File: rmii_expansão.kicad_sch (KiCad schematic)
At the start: 6 parts, among them CN3 100nf, J19 Bus_PCI_Express_Mini

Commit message: 21082026/G
falta muita coisa
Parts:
- removed J19: Bus_PCI_Express_Mini, Connector_PCBEdge:BUS_PCI_Express_Mini_Full, symbol Connector:Bus_PCI_Express_Mini
- added J19: ETH, symbol Connector_Generic:Conn_02x10_Row_Letter_First
- renumbered C102 to C100, D8 to D7
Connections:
- net GND: now also J19.a10 (Pin_a10), J19.a2 (Pin_a2), J19.a4 (Pin_a4), J19.a6 (Pin_a6), J19.a8 (Pin_a8), J19.b10 (Pin_b10), J19.b2 (Pin_b2), J19.b4 (Pin_b4), J19.b6 (Pin_b6), J19.b8 (Pin_b8)
- net SUB_RMII_CRS_DV: now also J19.a5 (Pin_a5)
- net SUB_RMII_RXD0: now also J19.b5 (Pin_b5)
- net SUB_RMII_RXD1: now also J19.a7 (Pin_a7)
- net SUB_RMII_TXD0: now also J19.a9 (Pin_a9)
- net SUB_RMII_TXD1: now also J19.b3 (Pin_b3)
- net SUB_RMII_TXEN: now also J19.a3 (Pin_a3)
- net vcc_RMII: now also J19.a1 (Pin_a1), J19.b1 (Pin_b1)
- new net SUB_GPIO_1: J19.b7 (Pin_b7)
- new net SUB_GPIO_2: J19.b9 (Pin_b9)
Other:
- moved on the sheet: D7, F11

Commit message: 29082026/I
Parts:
- CN3: jlc_pcb: C346191 -> C307348; mouser: (none) -> 187-CL10B104KB8WPNC; mpn CA0612MRX7R7BB104 -> CL10B104KB8WPNC
- J19: footprint (none) -> Connector_PinHeader_2.54mm:PinHeader_2x10_P2.54mm_Horizontal; Descrição (none) -> o da lcsc e da mouser sâo diferente; jlc_pcb: (none) -> C53207373; mouser: (none) -> 649-68021-120HLF; mpn (none) -> PZ-2.54-2*10-8.5-WZ
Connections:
- net GND: now also J19.a9 (Pin_a9), J19.b1 (Pin_b1), J19.b3 (Pin_b3), J19.b5 (Pin_b5), J19.b7 (Pin_b7), J19.b9 (Pin_b9); no longer J19.a10 (Pin_a10), J19.b10 (Pin_b10), J19.b2 (Pin_b2), J19.b4 (Pin_b4), J19.b6 (Pin_b6), J19.b8 (Pin_b8)
- net SUB_GPIO_1: now also J19.b6 (Pin_b6); no longer J19.b7 (Pin_b7)
- net SUB_GPIO_2: now also J19.b8 (Pin_b8); no longer J19.b9 (Pin_b9)
- net SUB_RMII_CRS_DV: now also J19.a3 (Pin_a3); no longer J19.a5 (Pin_a5)
- net SUB_RMII_RXD0: now also J19.b4 (Pin_b4); no longer J19.b5 (Pin_b5)
- net SUB_RMII_RXD1: now also J19.a5 (Pin_a5); no longer J19.a7 (Pin_a7)
- net SUB_RMII_TXD0: now also J19.a7 (Pin_a7); no longer J19.a9 (Pin_a9)
- net SUB_RMII_TXD1: now also J19.b2 (Pin_b2); no longer J19.b3 (Pin_b3)
- net SUB_RMII_TXEN: now also J19.a1 (Pin_a1); no longer J19.a3 (Pin_a3)
- net vcc_RMII: now also J19.a10 (Pin_a10), J19.b10 (Pin_b10); no longer J19.a1 (Pin_a1), J19.b1 (Pin_b1)
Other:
- company: (none) -> ---
- title: (none) -> expansão com ethernet
- moved on the sheet: D7, F11, J19

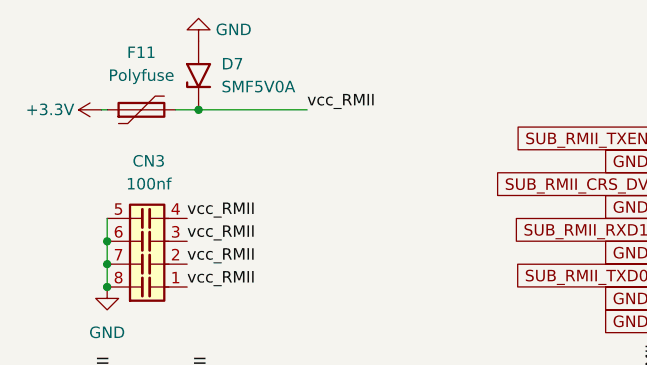
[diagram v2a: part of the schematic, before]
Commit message: o .bom não foi terminado
O desafio e todo custar menos de 150 dólares(eua) e menos de 1000r(reais)
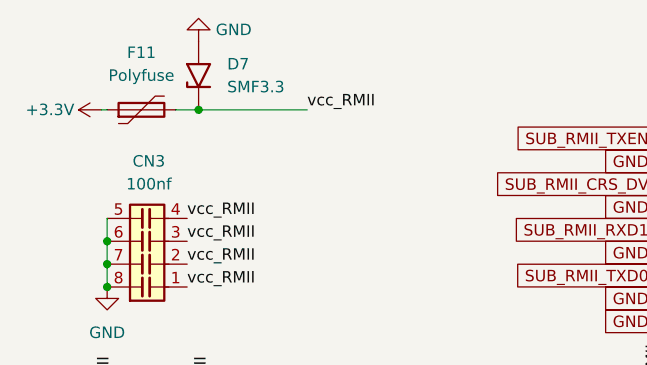
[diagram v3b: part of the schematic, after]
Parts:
- C100, C99: footprint (none) -> Capacitor_SMD:C_1206_3216Metric_Pad1.33x1.80mm_HandSolder; jlc_pcb: (none) -> C13585; mouser: (none) -> 187-CL31B106KLK6PNE; mpn (none) -> CL31A106KBHNNNE
- D7: value SMF5V0A -> SMF3.3
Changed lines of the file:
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@@
+	)
+	(junction
+		(at 33.02 33.02)
+		(diameter 0)
+		(color 0 0 0 0)
 	)
 	(junction
@@
 	)
 	(junction
-		(at 33.02 33.02)
-		(diameter 0)
-		(color 0 0 0 0)
-	)
-	(junction
 		(at 22.86 50.165)
 		(diameter 0)
@@
 	(wire
 		(pts
-			(xy 33.02 33.02) (xy 45.085 33.02)
+			(xy 30.48 33.02) (xy 33.02 33.02)
 		)
 		(stroke
@@
 	(wire
 		(pts
-			(xy 33.02 33.02) (xy 30.48 33.02)
+			(xy 22.86 50.165) (xy 22.86 52.705)
 		)
 		(stroke
@@
 	(wire
 		(pts
-			(xy 22.86 50.165) (xy 22.86 52.705)
+			(xy 33.02 33.02) (xy 45.085 33.02)
 		)
 		(stroke
@@
 	)
 	(symbol
+		(lib_id "Diode:SMF5V0A")
+		(at 33.02 29.21 90)
+		(unit 1)
+		(body_style 1)
+		(exclude_from_sim no)
+		(in_bom yes)
+		(on_board yes)
+		(in_pos_files yes)
+		(dnp no)
+		(fields_autoplaced yes)
+		(property "Reference" "D7"
+			(at 36.195 27.9399 90)
+			(show_name no)
+			(do_not_autoplace no)
+			(effects
+				(font
+					(size 1.27 1.27)
+				)
+				(justify right)
+			)
+		)
+		(property "Value" "SMF3.3"
+			(at 36.195 30.4799 90)
+			(show_name no)
+			(do_not_autoplace no)
+			(effects
+				(font
+					(size 1.27 1.27)
+				)
+				(justify right)
+			)
+		)
+		(property "Footprint" "Diode_SMD:D_SMF"
+			(at 38.1 29.21 0)
+			(hide yes)
+			(show_name no)
+			(do_not_autoplace no)
+			(effects
+				(font
+					(size 1.27 1.27)
+				)
+			)
+		)
+		(property "Datasheet" "https://www.vishay.com/doc?85881"
+			(at 33.02 30.48 0)
+			(hide yes)
+			(show_name no)
+			(do_not_autoplace no)
+			(effects
+				(font
+					(size 1.27 1.27)
+				)
+			)
+		)
+		(property "Description" "200W unidirectional Transil Transient Voltage Suppressor, 5Vrwm, SMF"
+			(at 33.02 29.21 0)
+			(hide yes)
+			(show_name no)
+			(do_not_autoplace no)
+			(effects
+				(font
+					(size 1.27 1.27)
+				)
+			)
+		)
+		(property "jlc_pcb:" ""
+			(at 33.02 29.21 0)
+			(hide yes)
+			(show_name no)
+			(do_not_autoplace no)
+			(effects
+				(font
+					(size 1.27 1.27)
+				)
+			)
+		)
+		(property "mpn" ""
+			(at 33.02 29.21 0)
+			(hide yes)
+			(show_name no)
+			(do_not_autoplace no)
+			(effects
+				(font
+					(size 1.27 1.27)
+				)
+			)
+		)
+		(property "mouser:" ""
+			(at 33.02 29.21 0)
+			(hide yes)
+			(show_name no)
+			(do_not_autoplace no)
+			(effects
+				(font
+					(size 1.27 1.27)
+				)
+			)
+		)
+		(property "Descrição" ""
+			(at 33.02 29.21 0)
+			(hide yes)
+			(show_name no)
+			(do_not_autoplace no)
+			(effects
+				(font
+					(size 1.27 1.27)
+				)
+			)
+		)
+		(pin "2"
+		)
+		(pin "1"
+		)
+		(instances
+			(project "hapia"
+				(path "/03882c7f-4c9a-440f-b893-3aa618650b49"
+					(reference "D7")
+					(unit 1)
+				)
+			)
+		)
+	)
+	(symbol
 		(lib_id "Device:C_Network04")
 		(at 27.94 47.625 90)
@@
 	)
 	(symbol
-		(lib_id "Diode:SMF5V0A")
-		(at 33.02 29.21 90)
-		(unit 1)
-		(body_style 1)
-		(exclude_from_sim no)
-		(in_bom yes)
-		(on_board yes)
-		(in_pos_files yes)
-		(dnp no)
-		(fields_autoplaced yes)
-		(property "Reference" "D7"
-			(at 35.56 27.9399 90)
-			(show_name no)
-			(do_not_autoplace no)
-			(effects
-				(font
-					(size 1.27 1.27)
-				)
-				(justify right)
-			)
-		)
-		(property "Value" "SMF5V0A"
-			(at 35.56 30.4799 90)
-			(show_name no)
-			(do_not_autoplace no)
-			(effects
-				(font
-					(size 1.27 1.27)
-				)
-				(justify right)
-			)
-		)
-		(property "Footprint" "Diode_SMD:D_SMF"
-			(at 38.1 29.21 0)
-			(hide yes)
-			(show_name no)
-			(do_not_autoplace no)
-			(effects
-				(font
-					(size 1.27 1.27)
-				)
-			)
-		)
-		(property "Datasheet" "https://www.vishay.com/doc?85881"
-			(at 33.02 30.48 0)
-			(hide yes)
-			(show_name no)
-			(do_not_autoplace no)
-			(effects
-				(font
-					(size 1.27 1.27)
-				)
-			)
-		)
-		(property "Description" "200W unidirectional Transil Transient Voltage Suppressor, 5Vrwm, SMF"
-			(at 33.02 29.21 0)
-			(hide yes)
-			(show_name no)
-			(do_not_autoplace no)
-			(effects
-				(font
-					(size 1.27 1.27)
-				)
-			)
-		)
-		(pin "2"
-		)
-		(pin "1"
-		)
-		(instances
-			(project "hapia"
-				(path "/03882c7f-4c9a-440f-b893-3aa618650b49"
-					(reference "D7")
-					(unit 1)
-				)
-			)
-		)
-	)
-	(symbol
 		(lib_id "Device:C")
 		(at 34.29 71.755 0)
@@
 			)
 		)
-		(property "Footprint" ""
+		(property "Footprint" "Capacitor_SMD:C_1206_3216Metric_Pad1.33x1.80mm_HandSolder"
 			(at 35.2552 75.565 0)
 			(hide yes)
@@
 			)
 		)
-		(property "Datasheet" ""
+		(property "Datasheet" "https://www.lcsc.com/datasheet/C13585.pdf?spm=wm.sxq.inf.ggs___wm.fly.bg.1.xh&lcsc_vid=RFYLUFJeFgBYVgUARVEKU1ZUEwNcUQJQEVkIVlNSQgIxVlNeQFhbU1VUQFRWUTsOAxUeFF5JWBYZEEoKFBINSQcJGk4NBhADEA4cHktRR1NADxALGw%3D%3D"
 			(at 34.29 71.755 0)
 			(hide yes)
@@
 		)
 		(property "Description" "Unpolarized capacitor"
+			(at 34.29 71.755 0)
+			(hide yes)
+			(show_name no)
+			(do_not_autoplace no)
+			(effects
+				(font
+					(size 1.27 1.27)
+				)
+			)
+		)
+		(property "jlc_pcb:" "C13585"
+			(at 34.29 71.755 0)
+			(hide yes)
+			(show_name no)
+			(do_not_autoplace no)
+			(effects
+				(font
+					(size 1.27 1.27)
+				)
+			)
+		)
+		(property "mouser:" "187-CL31B106KLK6PNE"
+			(at 34.29 71.755 0)
+			(hide yes)
+			(show_name no)
+			(do_not_autoplace no)
+			(effects
+				(font
+					(size 1.27 1.27)
+				)
+			)
+		)
+		(property "mpn" "CL31A106KBHNNNE"
 			(at 34.29 71.755 0)
 			(hide yes)
@@
 			)
 		)
-		(property "Footprint" ""
+		(property "Footprint" "Capacitor_SMD:C_1206_3216Metric_Pad1.33x1.80mm_HandSolder"
 			(at 24.4602 75.565 0)
 			(hide yes)
@@
 			)
 		)
-		(property "Datasheet" ""
+		(property "Datasheet" "https://www.lcsc.com/datasheet/C13585.pdf?spm=wm.sxq.inf.ggs___wm.fly.bg.1.xh&lcsc_vid=RFYLUFJeFgBYVgUARVEKU1ZUEwNcUQJQEVkIVlNSQgIxVlNeQFhbU1VUQFRWUTsOAxUeFF5JWBYZEEoKFBINSQcJGk4NBhADEA4cHktRR1NADxALGw%3D%3D"
 			(at 23.495 71.755 0)
 			(hide yes)
@@
 			(at 23.495 71.755 0)
 			(hide yes)
+			(show_name no)
+			(do_not_autoplace no)
+			(effects
+				(font
+					(size 1.27 1.27)
+				)
+			)
+		)
+		(property "jlc_pcb:" "C13585"
+			(at 23.495 71.755 0)
+			(hide yes)
+			(show_name no)
+			(do_not_autoplace no)
+			(effects
+				(font
+					(size 1.27 1.27)
+				)
+			)
+		)
+		(property "mouser:" "187-CL31B106KLK6PNE"
+			(at 23.495 71.755 0)
+			(hide yes)
+			(show_name no)
+			(do_not_autoplace no)
+			(effects
+				(font
+					(size 1.27 1.27)
+				)
+			)
+		)
+		(property "mpn" "CL31A106KBHNNNE"
+			(at 23.495 71.755 0)
+			(hide yes)
